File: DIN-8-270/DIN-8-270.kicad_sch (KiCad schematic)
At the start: 3 parts, among them J1 Socket, J2 Pins, J3 Breakout

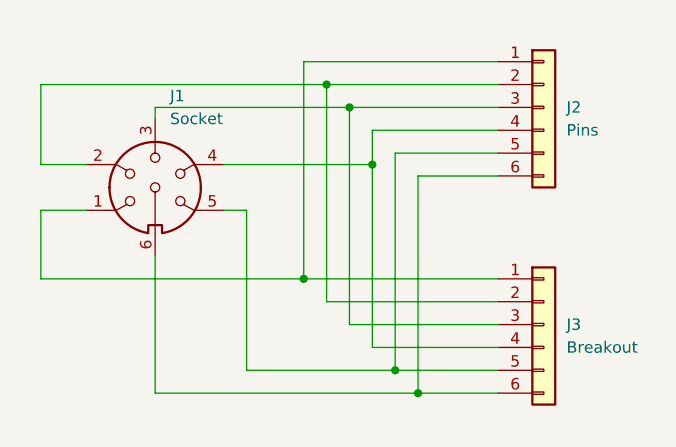
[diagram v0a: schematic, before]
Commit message: Improve layouts, add DIN-8 270° board.
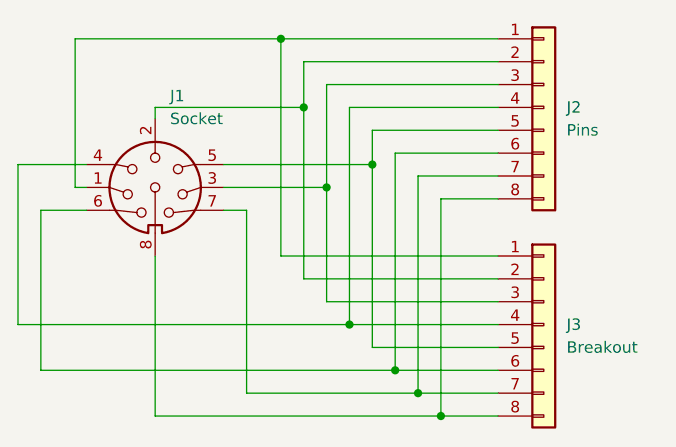
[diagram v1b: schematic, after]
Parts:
- J1: footprint T-Pau:DIN-6 -> T-Pau:DIN-8-270; symbol Connector:DIN-6 -> Connector:DIN-8
- J2, J3: footprint Connector_PinHeader_2.54mm:PinHeader_1x06_P2.54mm_Vertical -> Connector_PinHeader_2.54mm:PinHeader_1x08_P2.54mm_Vertical; symbol Connector_Generic:Conn_01x06 -> Connector_Generic:Conn_01x08
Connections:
- new net: J1.7, J2.7 (Pin_7), J3.7 (Pin_7)
- new net: J1.8, J2.8 (Pin_8), J3.8 (Pin_8)
